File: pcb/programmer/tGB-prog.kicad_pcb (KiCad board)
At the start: 2 copper layers, 29 parts, among them J1 USB_B_Micro, J2 PROG_PORT, U1 FT232HL, Y1 FA238V 12MHz

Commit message: update pcb (wip)
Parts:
- moved FB3 43.7 mm to (68.5, 74.1)
- moved C16 43.1 mm to (76.0, 74.3), turned to 180 degrees
- moved C7 43.0 mm to (78.9, 74.2), turned to 180 degrees
- moved C5 42.9 mm to (82.0, 74.2), turned to 0 degrees
- moved C10 42.8 mm to (70.8, 82.0)
- moved C12 42.8 mm to (71.8, 82.0)
- moved FB2 42.8 mm to (69.4, 82.5)
- moved C14 42.7 mm to (71.2, 83.5)
- moved C15 42.7 mm to (81.2, 87.1)
- moved C2 42.7 mm to (79.7, 71.1)
- moved C9 42.4 mm to (69.9, 73.5)
- moved C4 42.4 mm to (79.7, 72.1)
- moved C13 42.4 mm to (70.0, 77.6), turned to 180 degrees
- moved U1 42.3 mm to (78.2, 80.1)
- moved R2 42.1 mm to (70.0, 78.7)
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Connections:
- D1 pad 1: /USB_DP -> GND
- D1 pad 2: GND -> /USB_DP
- J2 pad 6: /AD3 -> /AD2
- J2 pad 7: /AD2 -> /AD3
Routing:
- net GND: track 0.00 -> 20.5 mm, vias 0 -> 3
- net Net-(C8-Pad1): track 0.00 -> 8.27 mm
- net /VPHY: track 0.00 -> 7.98 mm
- net +3.3V: track 0.00 -> 6.59 mm
- net /VBUS: track 0.00 -> 6.10 mm
- net /VPLL: track 0.00 -> 5.03 mm
- net /USB_DM: track 0.00 -> 3.91 mm
- net /USB_DP: track 0.00 -> 3.91 mm
- net Net-(R2-Pad2): track 0.00 -> 3.82 mm
- net Net-(C9-Pad1): track 0.00 -> 3.48 mm
- net /VCCCORE: track 0.00 -> 3.42 mm
- net Net-(R3-Pad2): track 0.00 -> 2.78 mm
- net /VCCA: track 0.00 -> 2.17 mm
- net +5V: track 0.00 -> 1.74 mm
- added copper zone on F.Cu, net /USB_DM
- added copper zone on F.Cu, net /USB_DP
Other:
- board outline added: 25.2 x 31 mm

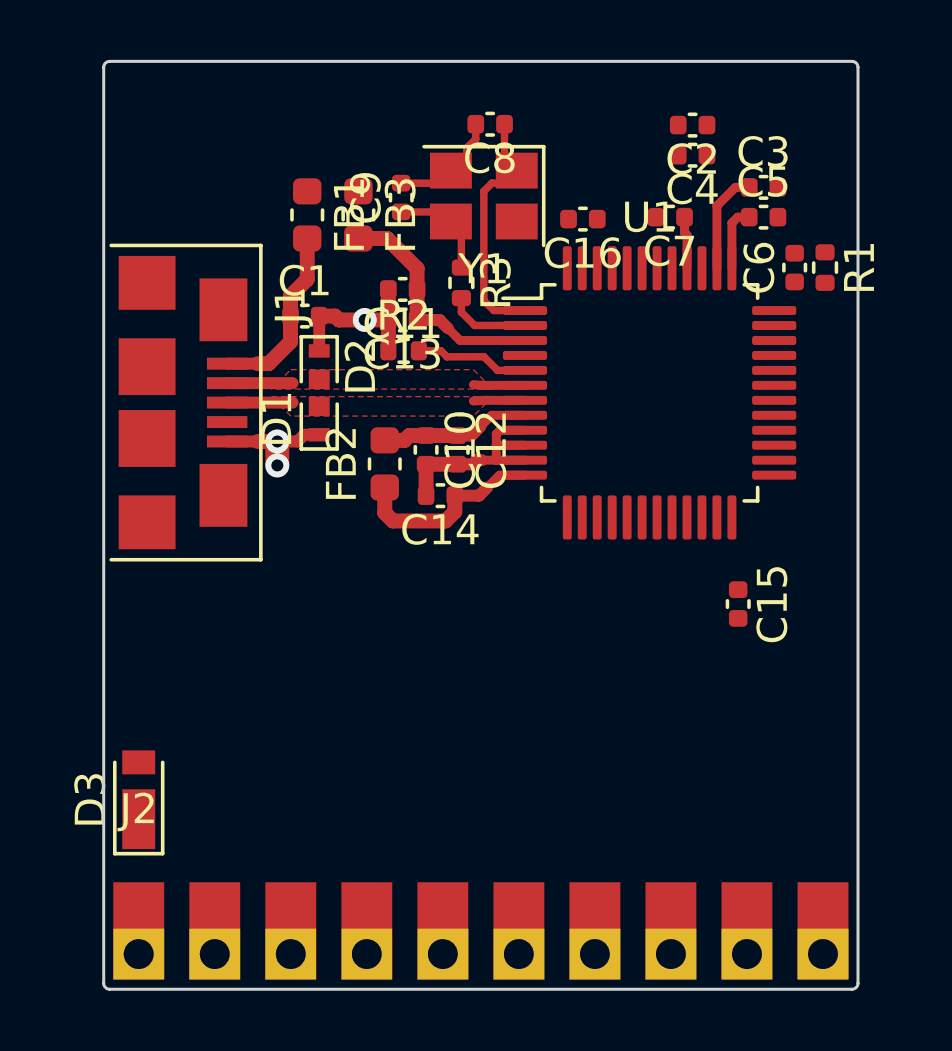
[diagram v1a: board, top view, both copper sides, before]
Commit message: complete placement and route of components, DRC passed with warnings
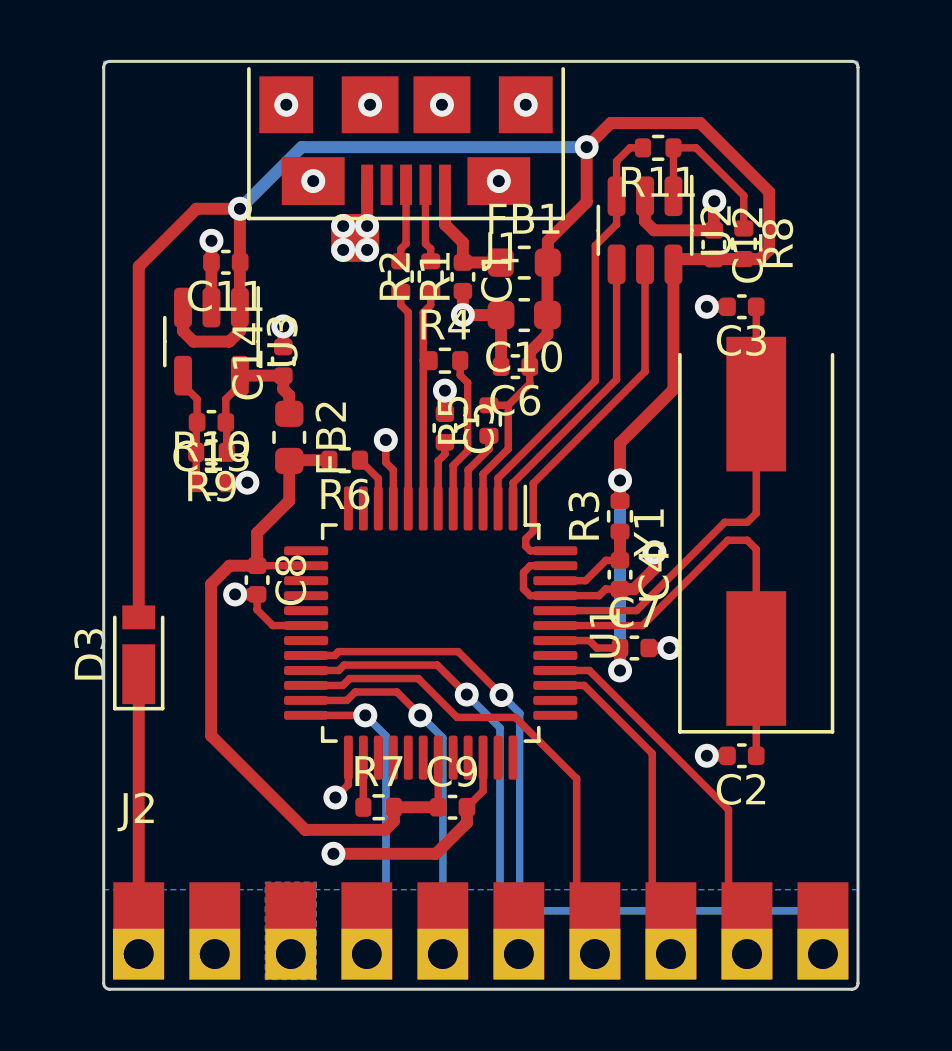
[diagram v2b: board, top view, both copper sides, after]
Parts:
- removed C15, C16: 0.1μF, Capacitor_SMD:C_0402_1005Metric
- removed D1, D2: DF2S23P2CTC, D_SOD-963:D_SOD-963
- removed FB3: 600Ω, Inductor_SMD:L_0603_1608Metric
- added R10: 68kΩ, Resistor_SMD:R_0402_1005Metric, F.Cu at (63.6, 83.1)
- added R11: 2.2kΩ, Resistor_SMD:R_0402_1005Metric, F.Cu at (78.5, 71.9)
- added R4: 1.5kΩ, Resistor_SMD:R_0402_1005Metric, F.Cu at (71.4, 79.0)
- added R5: 47kΩ, Resistor_SMD:R_0402_1005Metric, F.Cu at (72.9, 81.0)
- added R6: 47kΩ, Resistor_SMD:R_0402_1005Metric, F.Cu at (68.0, 82.3)
- added R7: 47kΩ, Resistor_SMD:R_0402_1005Metric, F.Cu at (69.2, 93.9)
- added R8: 10kΩ, Resistor_SMD:R_0402_1005Metric, F.Cu at (81.4, 75.1)
- added R9: 120kΩ, Resistor_SMD:R_0402_1005Metric, F.Cu at (63.6, 82.1)
- added U2: 93LC56BT-I/OT, Package_TO_SOT_SMD:SOT-23-6, F.Cu at (78.1, 74.6)
- added U3: TPS79901DDCR, Package_TO_SOT_SMD:SOT-23-5, F.Cu at (63.6, 78.4)
- C10: value 4.7μF -> 10μF; footprint Capacitor_SMD:C_0402_1005Metric -> Capacitor_SMD:C_0603_1608Metric
- C11: value 4.7μF -> 0.1μF
- C13, C3: value 0.1μF -> 47pF
- C14: value 0.1μF -> 4.7μF
- C2: value 4.7μF -> 47pF
- C5: value 0.1μF -> 33nF
- C6: value 10nF -> 0.1μF
- C8, C9: value 15pF -> 0.1μF
- FB1, FB2: value 600Ω -> MPZ1608S601ATA00
- J1: value USB_B_Micro -> ZX62-B-5PA(33)
- R1: value 10kΩ -> 27Ω
- R2: value 12kΩ -> 27Ω
- R3: value 100Ω -> 470Ω
- U1: value FT232HL -> FT2232D
- Y1: value FA238V 12MHz -> ML49G 6MHz; footprint Crystal:Crystal_SMD_3225-4Pin_3.2x2.5mm -> Crystal:Crystal_SMD_HC49-SD
- moved C2 21.1 mm to (81.3, 92.2)
- moved C9 20.4 mm to (71.7, 93.9), turned to 0 degrees
- moved C8 17.1 mm to (65.1, 86.3), turned to -90 degrees
- moved J1 15.2 mm to (70.1, 69.0), turned to 180 degrees
- moved C7 14.4 mm to (77.7, 88.6), turned to 0 degrees
- moved Y1 14.4 mm to (81.8, 84.7), turned to 90 degrees
- moved C4 14.2 mm to (77.2, 86.2), turned to -90 degrees
- moved R1 14.2 mm to (69.9, 76.2)
- moved C5 12.8 mm to (71.4, 81.2), turned to -90 degrees
- moved C12 11.0 mm to (80.4, 75.1)
- moved U1 10.9 mm to (70.9, 88.1), turned to -90 degrees
- moved C6 9.90 mm to (73.8, 79.2), turned to 180 degrees
- moved R3 9.43 mm to (77.2, 84.2), turned to 90 degrees
- moved FB1 7.42 mm to (74.0, 75.7), turned to 0 degrees
- moved C13 7.25 mm to (63.6, 81.1)
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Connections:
- net Net-(D3-Pad1) renamed /+5V_GB
- C10 pad 1: /VPLL -> +5V
- C11 pad 1: /VPHY -> +5V
- C12 pad 1: /VPLL -> GND
- C12 pad 2: GND -> +5V
- C13 pad 1: /VPHY -> /3V3VO
- C13 pad 2: GND -> Net-(C13-Pad2)
- C14 pad 1: +3.3V -> /3V3VO
- C2 pad 1: +3.3V -> Net-(C2-Pad1)
- C3 pad 1: /VCCCORE -> Net-(C3-Pad1)
- C4 pad 1: +3.3V -> /AVCC
- C5 pad 1: /VCCA -> GND
- C5 pad 2: GND -> Net-(C5-Pad2)
- C6 pad 1: /~{RESET} -> +5V
- C8 pad 1: Net-(C8-Pad1) -> +3V3
- C9 pad 1: Net-(C9-Pad1) -> +3V3
- FB1 pad 1: +5V -> /VBUS
- FB1 pad 2: /VBUS -> +5V
- FB2 pad 1: +3.3V -> /3V3VO
- FB2 pad 2: /VPLL -> +3V3
- J1 pad 2: /USB_DM -> Net-(J1-Pad2)
- J1 pad 3: /USB_DP -> Net-(J1-Pad3)
- J2 pad 10: /AD6 -> /~{CRESET}
- J2 pad 4: /AD0 -> /SCK
- J2 pad 5: /AD1 -> /MOSI
- J2 pad 6: /AD2 -> /SS
- J2 pad 7: /AD3 -> /MISO
- J2 pad 8: /AD4 -> /UART_RXD
- J2 pad 9: /AD5 -> /UART_TXD
- R1 pad 1: +3.3V -> Net-(J1-Pad3)
- R1 pad 2: /~{RESET} -> /USB_DM
- R2 pad 1: GND -> /USB_DP
- R2 pad 2: Net-(R2-Pad2) -> Net-(J1-Pad2)
- R3 pad 1: Net-(C9-Pad1) -> /AVCC
- R3 pad 2: Net-(R3-Pad2) -> +5V
- U1 pad 1: Net-(C8-Pad1) -> /EECLK
- U1 pad 10: GND -> Net-(R6-Pad1)
- U1 pad 11: GND -> unconnected-(U1-Pad11)
- U1 pad 12: +3.3V -> unconnected-(U1-Pad12)
- U1 pad 13: /AD0 -> unconnected-(U1-Pad13)
- U1 pad 14: /AD1 -> +3V3
- U1 pad 15: /AD2 -> unconnected-(U1-Pad15)
- U1 pad 16: /AD3 -> unconnected-(U1-Pad16)
- U1 pad 17: /AD4 -> unconnected-(U1-Pad17)
- U1 pad 18: /AD5 -> GND
- U1 pad 19: /AD6 -> unconnected-(U1-Pad19)
- U1 pad 2: Net-(R3-Pad2) -> /EEDATA
- U1 pad 20: unconnected-(U1-Pad20) -> /~{CRESET}
- U1 pad 21: unconnected-(U1-Pad21) -> /SS
- U1 pad 22: GND -> /MISO
- U1 pad 23: GND -> /MOSI
- U1 pad 24: +3.3V -> /SCK
- U1 pad 25: unconnected-(U1-Pad25) -> GND
- U1 pad 26: unconnected-(U1-Pad26) -> Net-(R7-Pad1)
- U1 pad 3: /VPHY -> +5V
- U1 pad 31: unconnected-(U1-Pad31) -> +3V3
- U1 pad 34: /~{RESET} -> GND
- U1 pad 35: GND -> unconnected-(U1-Pad35)
- U1 pad 36: GND -> unconnected-(U1-Pad36)
- U1 pad 37: /VCCA -> unconnected-(U1-Pad37)
- U1 pad 38: /VCCCORE -> unconnected-(U1-Pad38)
- U1 pad 39: +3.3V -> /UART_RXD
- U1 pad 4: GND -> Net-(R5-Pad1)
- U1 pad 40: +5V -> /UART_TXD
- U1 pad 41: GND -> unconnected-(U1-Pad41)
- U1 pad 42: GND -> +5V
- U1 pad 43: unconnected-(U1-Pad43) -> Net-(C2-Pad1)
- U1 pad 44: unconnected-(U1-Pad44) -> Net-(C3-Pad1)
- U1 pad 45: unconnected-(U1-Pad45) -> GND
- U1 pad 46: +3.3V -> /AVCC
- U1 pad 48: GND -> /EECS
- U1 pad 5: Net-(R2-Pad2) -> Net-(R4-Pad2)
- U1 pad 6: /USB_DM -> Net-(C5-Pad2)
- U1 pad 8: /VPLL -> /USB_DM
- Y1 pad 1: Net-(C8-Pad1) -> Net-(C2-Pad1)
- Y1 pad 2: GND -> Net-(C3-Pad1)
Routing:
- net +5V: track 1.74 -> 80.3 mm, vias 0 -> 4
- net /~{CRESET}: track 0.00 -> 25.7 mm, vias 0 -> 1
- net +3V3: track 0.00 -> 24.9 mm
- net GND: track 20.5 -> 40.4 mm, vias 3 -> 24
- net /MISO: track 0.00 -> 15.9 mm
- net /SS: track 0.00 -> 15.2 mm, vias 0 -> 1
- net Net-(C3-Pad1): track 0.00 -> 15.0 mm
- net Net-(C2-Pad1): track 0.00 -> 14.9 mm
- net /EEDATA: track 0.00 -> 14.3 mm
- net /MOSI: track 0.00 -> 12.5 mm, vias 0 -> 1
- net /EECS: track 0.00 -> 12.1 mm
- net /UART_TXD: track 0.00 -> 12.0 mm
- net /SCK: track 0.00 -> 10.5 mm, vias 0 -> 1
- net /UART_RXD: track 0.00 -> 10.4 mm
- net /EECLK: track 0.00 -> 9.59 mm
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- added copper zone on B.Cu, net GND
- removed copper zone on F.Cu, net /USB_DM
- removed copper zone on F.Cu, net /USB_DP

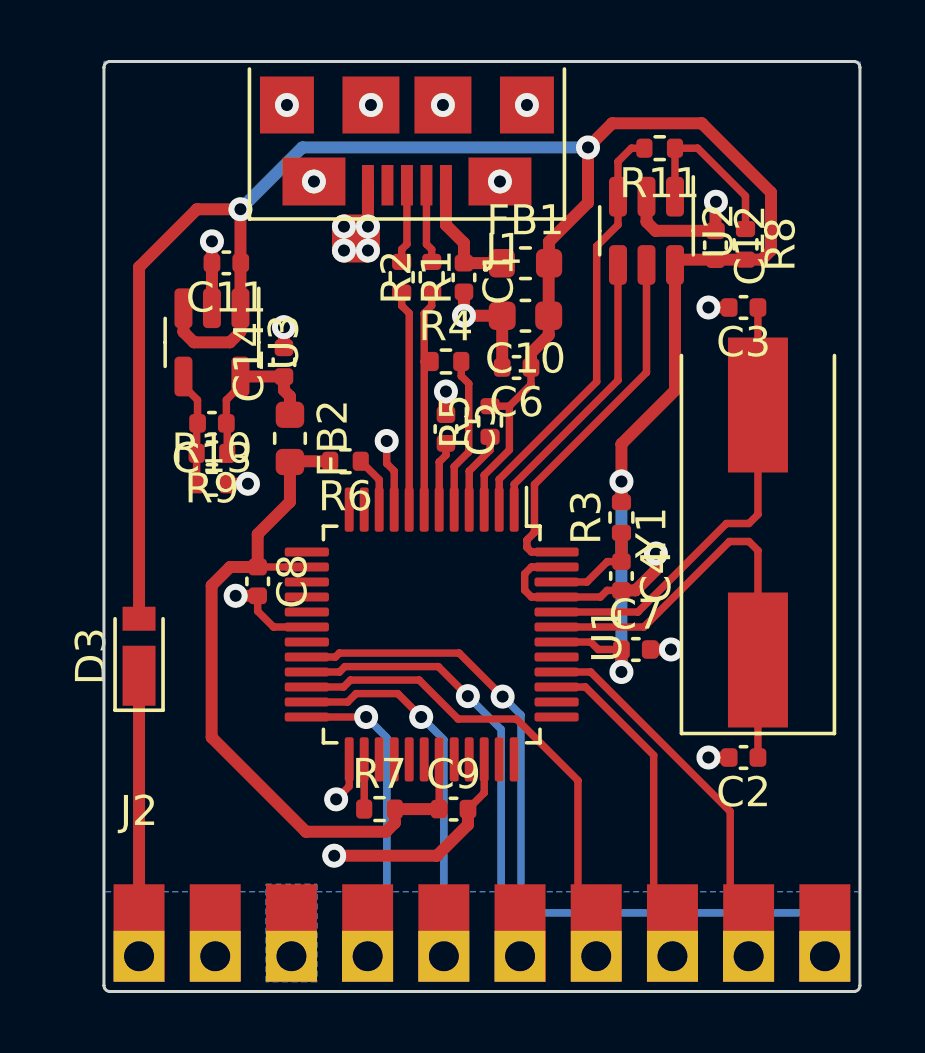
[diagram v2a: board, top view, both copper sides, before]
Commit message: fix silkscreens
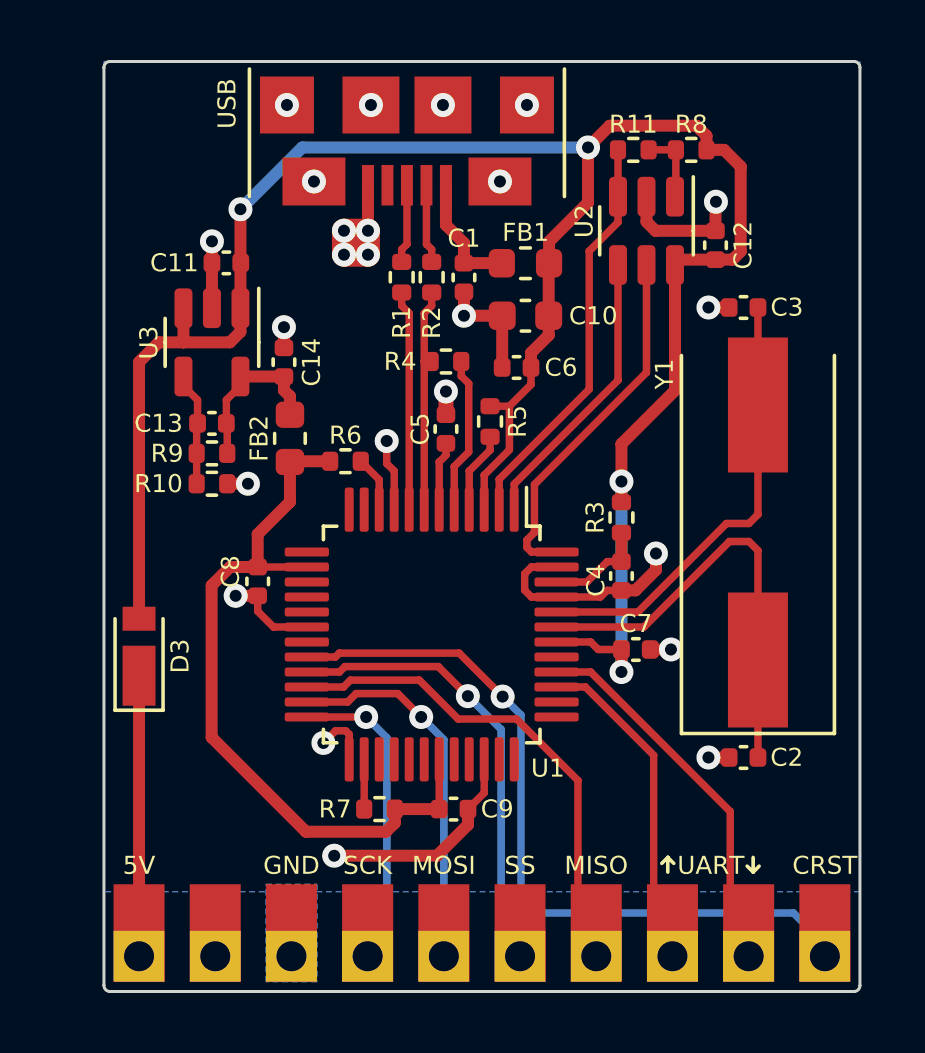
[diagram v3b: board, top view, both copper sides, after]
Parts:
- moved R8 3.63 mm to (79.6, 71.9), turned to 0 degrees
- moved R11 0.88 mm to (77.6, 71.9)
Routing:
- net +5V: track 80.3 -> 73.6 mm
- net Net-(R11-Pad1): track 5.73 -> 2.48 mm
- net /EEDATA: track 14.3 -> 13.6 mm
- net GND: track 40.4 -> 41.0 mm
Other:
- board text added: "5V"
- board text added: "CRST"
- board text added: "GND"
- board text added: "MISO"
- board text added: "MOSI"
- board text added: "SCK"
- board text added: "SS"
- board text added: "UART"
- board text added: "USB"

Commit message: add silkscreen of board name
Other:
- board text added: "tGB Programmer Rev.A 2022-09"
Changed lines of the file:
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@@
     )
   )
+  (gr_line (start 73.7 84.6) (end 73.7 84.1) (layer "B.SilkS") (width 0.15))
   (gr_line (start 78.995 97.23) (end 78.795 97.03) (layer "B.SilkS") (width 0.12))
   (gr_line (start 81.84 97.32) (end 81.64 97.52) (layer "B.SilkS") (width 0.12))
+  (gr_line (start 73 84.6) (end 73 84.1) (layer "B.SilkS") (width 0.15))
+  (gr_line (start 73.7 87.3) (end 73.7 86.8) (layer "B.SilkS") (width 0.15))
   (gr_line (start 81.64 97.03) (end 81.64 97.52) (layer "B.SilkS") (width 0.12))
   (gr_line (start 78.795 97.03) (end 78.595 97.23) (layer "B.SilkS") (width 0.12))
   (gr_line (start 81.64 97.52) (end 81.44 97.32) (layer "B.SilkS") (width 0.12))
   (gr_line (start 78.795 97.03) (end 78.795 97.52) (layer "B.SilkS") (width 0.12))
+  (gr_line (start 73 87.3) (end 73 86.8) (layer "B.SilkS") (width 0.15))
+  (gr_rect (start 74.1 84.6) (end 71.1 86.8) (layer "B.SilkS") (width 0.15) (fill none))
+  (gr_line (start 72.2 84.6) (end 72.2 84.1) (layer "B.SilkS") (width 0.15))
+  (gr_line (start 71.3 69.95) (end 75.35 69.95) (layer "B.SilkS") (width 0.15))
+  (gr_poly
+    (pts
+      (xy 73.4 83.9)
+      (xy 72.3 83.7)
+      (xy 72.6 85.4)
+      (xy 71.6 83.3)
+      (xy 72.7 83.5)
+      (xy 72.4 81.8)
+    ) (layer "B.SilkS") (width 0.15) (fill solid))
+  (gr_line (start 71.5 84.6) (end 71.5 84.1) (layer "B.SilkS") (width 0.15))
+  (gr_line (start 68.9 69.95) (end 64.85 69.95) (layer "B.SilkS") (width 0.15))
+  (gr_line (start 72.2 87.3) (end 72.2 86.8) (layer "B.SilkS") (width 0.15))
+  (gr_line (start 71.5 87.3) (end 71.5 86.8) (layer "B.SilkS") (width 0.15))
   (gr_line (start 78.795 95.53) (end 78.795 96.02) (layer "F.SilkS") (width 0.12))
   (gr_line (start 78.795 95.53) (end 78.995 95.73) (layer "F.SilkS") (width 0.12))
@@
   (gr_line (start 81.64 96.02) (end 81.84 95.82) (layer "F.SilkS") (width 0.12))
   (gr_line (start 60.2 100) (end 85 100) (layer "Edge.Cuts") (width 0.1))
+  (gr_arc (start 60 69.2) (mid 60.058579 69.058579) (end 60.2 69) (layer "Edge.Cuts") (width 0.1))
   (gr_line (start 85 69) (end 60.2 69) (layer "Edge.Cuts") (width 0.1))
   (gr_arc (start 85.2 99.8) (mid 85.141421 99.941421) (end 85 100) (layer "Edge.Cuts") (width 0.1))
   (gr_line (start 85.2 99.8) (end 85.2 69.2) (layer "Edge.Cuts") (width 0.1))
   (gr_arc (start 85 69) (mid 85.141421 69.058579) (end 85.2 69.2) (layer "Edge.Cuts") (width 0.1))
-  (gr_arc (start 60.2 100) (mid 60.058579 99.941421) (end 60 99.8) (layer "Edge.Cuts") (width 0.1))
+  (gr_arc (start 60.200001 99.999999) (mid 60.05858 99.94142) (end 60.000001 99.799999) (layer "Edge.Cuts") (width 0.1))
   (gr_line (start 60 69.2) (end 60 99.8) (layer "Edge.Cuts") (width 0.1))
-  (gr_arc (start 60 69.2) (mid 60.058579 69.058579) (end 60.2 69) (layer "Edge.Cuts") (width 0.1))
   (gr_text "MOSI" (at 71.33 97.3) (layer "B.SilkS")
-    (effects (font (size 0.6 0.6) (thickness 0.12)) (justify mirror))
-  )
-  (gr_text "USB" (at 70.095 69.69) (layer "B.SilkS")
     (effects (font (size 0.6 0.6) (thickness 0.12)) (justify mirror))
   )
@@
   )
   (gr_text "CRST" (at 84.03 97.3) (layer "B.SilkS")
+    (effects (font (size 0.6 0.6) (thickness 0.12)) (justify mirror))
+  )
+  (gr_text "tGB Programmer    Rev.A  2022-09" (at 84.2 84.5 270) (layer "B.SilkS")
     (effects (font (size 0.6 0.6) (thickness 0.12)) (justify mirror))
   )
@@
     (effects (font (size 0.6 0.6) (thickness 0.12)) (justify mirror))
   )
+  (gr_text "USB" (at 70.1 70) (layer "B.SilkS")
+    (effects (font (size 0.6 0.6) (thickness 0.12)) (justify mirror))
+  )
